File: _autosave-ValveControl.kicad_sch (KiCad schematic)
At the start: 30 parts, among them J10 Valve_1_PWR, J11 Valve_1_PWR, J6 Valve_1_PWR, J7 Valve_1_PWR, J8 Valve_1_PWR, J9 Valve_1_PWR, Q1 BSS138, Q2 BSS138, Q3 BSS138, Q4 BSS138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

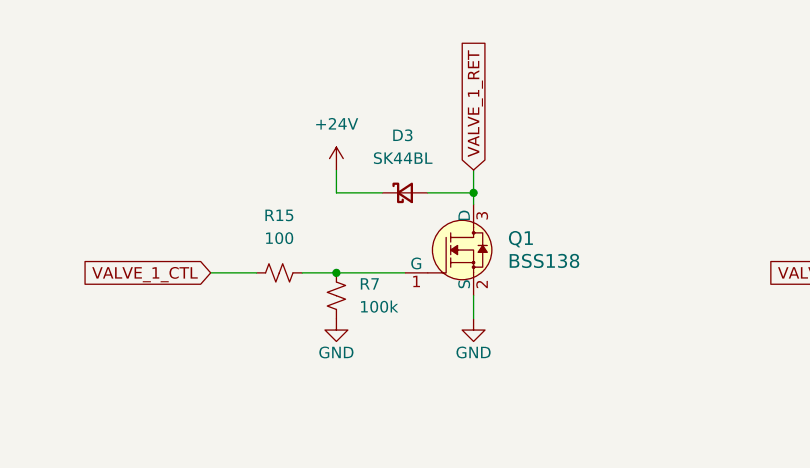
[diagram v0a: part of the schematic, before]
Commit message: Add valve control
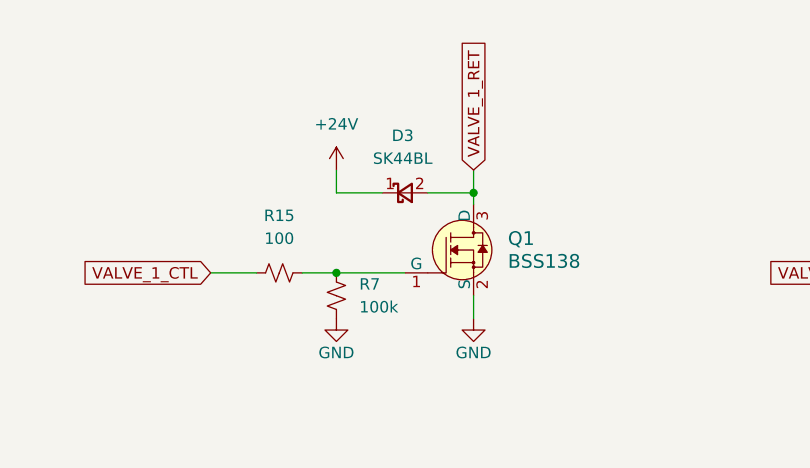
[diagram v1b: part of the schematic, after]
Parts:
- D3, D4, D5, D6, D7, D8: footprint (none) -> Diode_SMD:D_SMB
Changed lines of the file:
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@@
 	)
 	(symbol
+		(lib_name "D_Schottky_Small_1")
 		(lib_id "Device:D_Schottky_Small")
 		(at 80.01 53.34 0)
@@
 			)
 		)
-		(property "Footprint" ""
+		(property "Footprint" "Diode_SMD:D_SMB"
 			(at 80.01 53.34 90)
 			(effects
@@
 			)
 		)
-		(property "Footprint" ""
+		(property "Footprint" "Diode_SMD:D_SMB"
 			(at 156.21 53.34 90)
 			(effects
@@
 			)
 		)
-		(property "Footprint" ""
+		(property "Footprint" "Diode_SMD:D_SMB"
 			(at 156.21 101.6 90)
 			(effects
@@
 			)
 		)
-		(property "Footprint" ""
+		(property "Footprint" "Diode_SMD:D_SMB"
 			(at 80.01 101.6 90)
 			(effects
@@
 			)
 		)
-		(property "Footprint" ""
+		(property "Footprint" "Diode_SMD:D_SMB"
 			(at 226.06 101.6 90)
 			(effects
@@
 			)
 		)
-		(property "Footprint" ""
+		(property "Footprint" "Diode_SMD:D_SMB"
 			(at 226.06 53.34 90)
 			(effects
